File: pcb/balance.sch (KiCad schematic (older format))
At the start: 41 parts, among them J1 Resistive_Touch, J2 JTAG, J3 Conn_01x04_Male, J4 PJ-102AH, J5 UART (Bluetooth), J6 Conn_02x03_Top_Bottom, J7 Conn_02x03_Top_Bottom, M1 Motor_Servo, M2 Motor_Servo, Q1 MMBT3904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

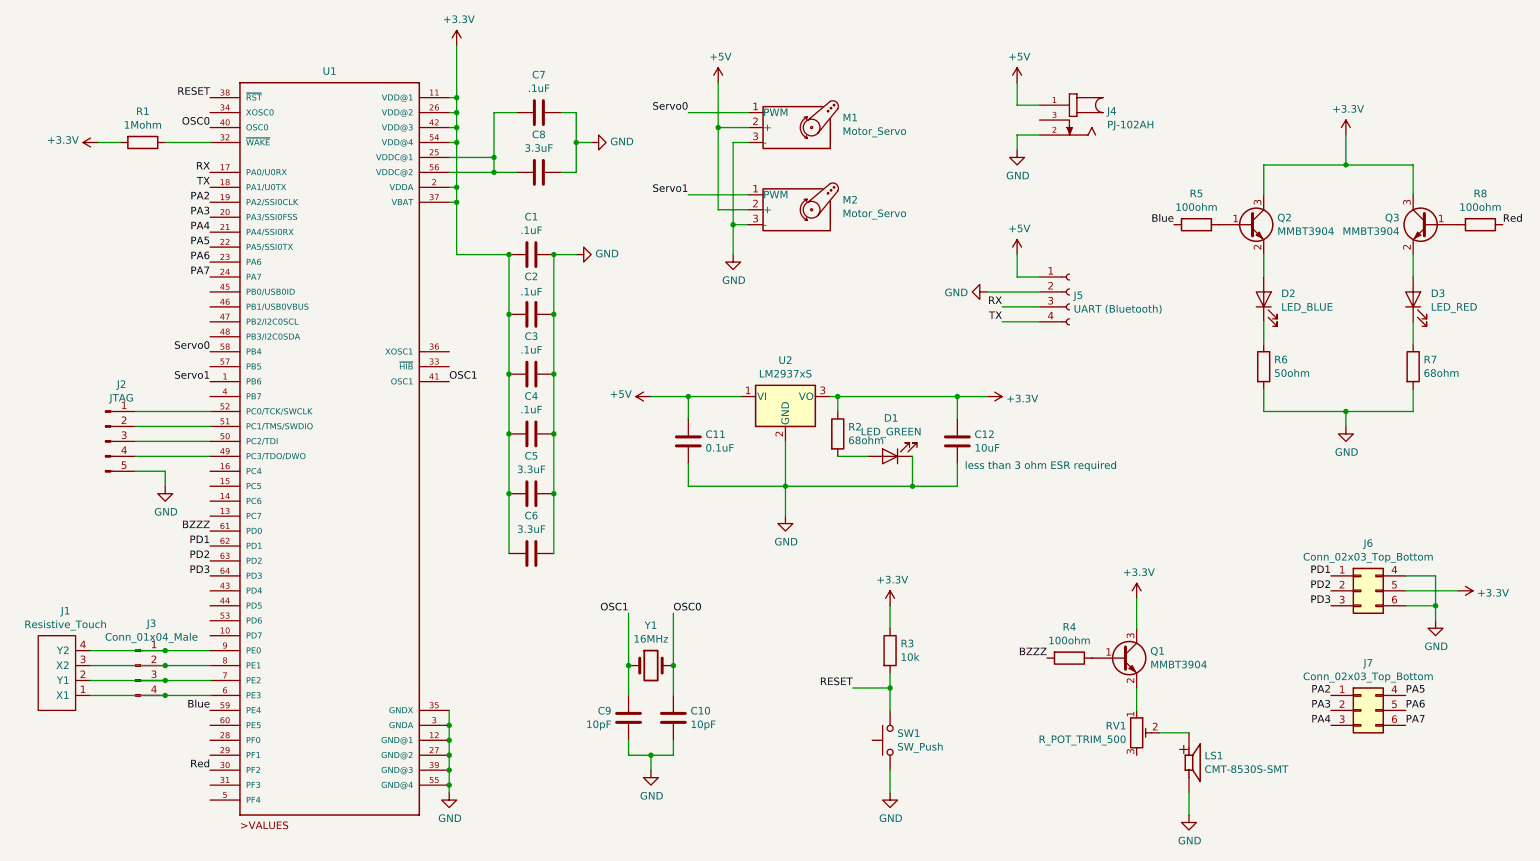
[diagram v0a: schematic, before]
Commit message: Modify component placement and fix transistor circuits
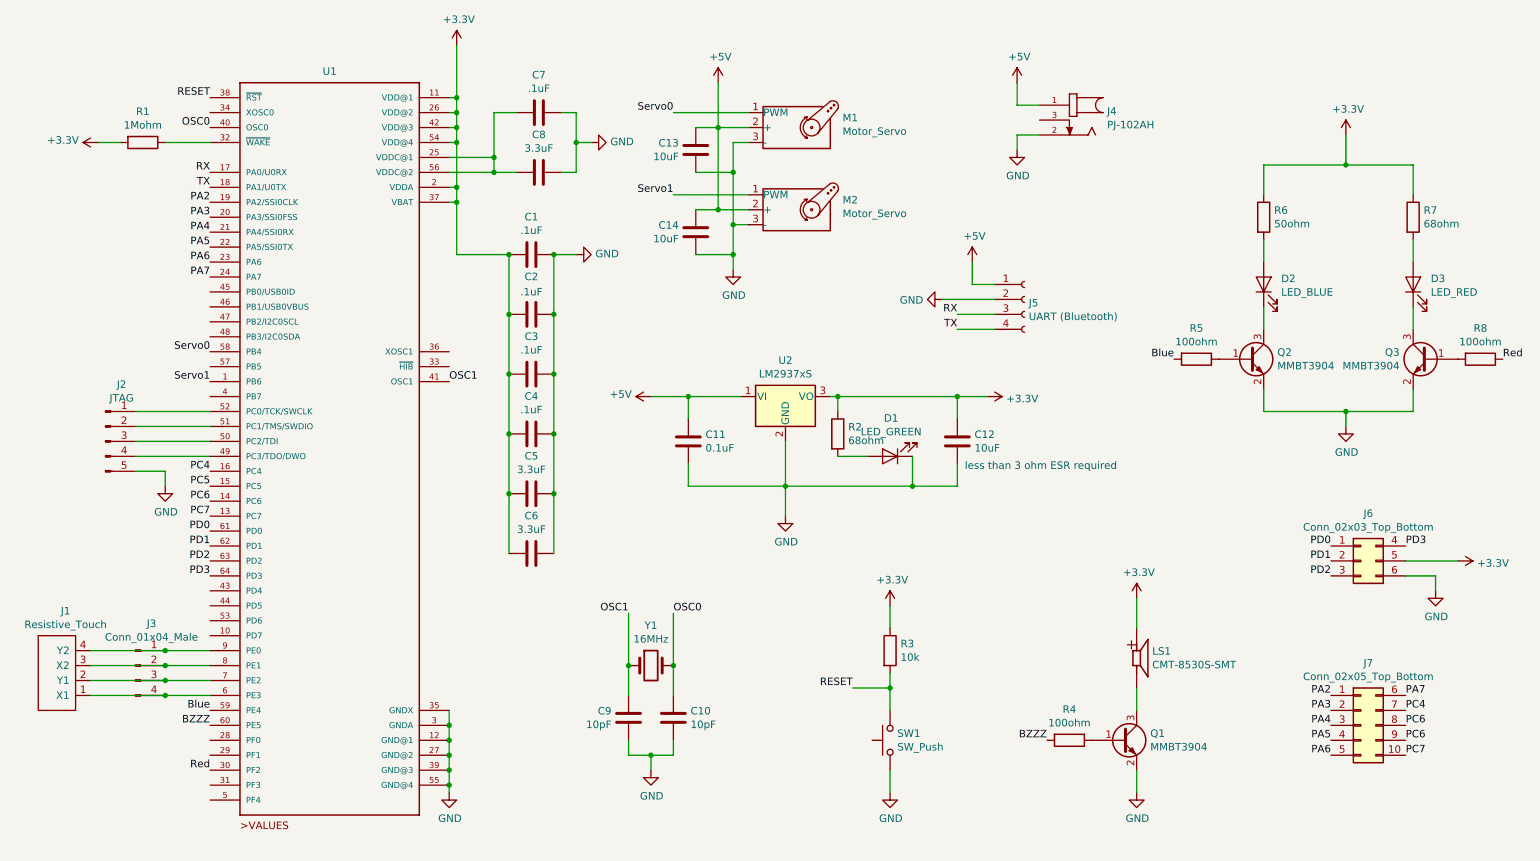
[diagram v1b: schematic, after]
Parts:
- removed J7: Conn_02x03_Top_Bottom, Connector_PinHeader_2.54mm:PinHeader_2x03_P2.54mm_Vertical, symbol Connector_Generic:Conn_02x03_Top_Bottom
- removed RV1: R_POT_TRIM_500, Potentiometer_SMD:Potentiometer_Bourns_3314J_Vertical, symbol Device:R_POT_TRIM
- added C13, C14: 10uF, Capacitor_SMD:C_0805_2012Metric, symbol Device:C
- added J7: Conn_02x05_Top_Bottom, Connector_PinHeader_2.54mm:PinHeader_2x05_P2.54mm_Vertical, symbol Connector_Generic:Conn_02x05_Top_Bottom
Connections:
- net +3V3: now also LS1.P, R6.1, R7.1; no longer Q1.3 (C), Q2.3 (C), Q3.3 (C)
- net +5V: now also C13.2, C14.2
- net BZZZ: now also U1.60 (PE5); no longer U1.61 (PD0)
- net GND: now also Q1.2 (E), Q2.2 (E), Q3.2 (E), C13.1, C14.1; no longer J6.4 (Pin_4), LS1.N, R6.2, R7.2
- net PA2: now also J7.1 (Pin_1)
- net PA3: now also J7.2 (Pin_2)
- net PA4: now also J7.3 (Pin_3)
- net PA5: now also J7.4 (Pin_4)
- net PA6: now also J7.5 (Pin_5)
- net PA7: now also J7.6 (Pin_6)
- net PD1: now also J6.2 (Pin_2); no longer J6.1 (Pin_1)
- net PD2: now also J6.3 (Pin_3); no longer J6.2 (Pin_2)
- net PD3: now also J6.4 (Pin_4); no longer J6.3 (Pin_3)
- net PC7: now reaches U1.13 (PC7)
- net PC7: now also J7.10 (Pin_10)
- net PC6: now reaches U1.14 (PC6)
- net PC6: now also J7.8 (Pin_8), J7.9 (Pin_9)
- net PC5: now reaches U1.15 (PC5)
- net PC4: now reaches U1.16 (PC4)
- net PC4: now also J7.7 (Pin_7)
- net at D2.2 (A): now also R6.2; no longer Q2.2 (E)
- net at D2.1 (K): now also Q2.3 (C); no longer R6.1
- net at D3.2 (A): now also R7.2; no longer Q3.2 (E)
- net at D3.1 (K): now also Q3.3 (C); no longer R7.1
- new net: LS1.N, Q1.3 (C)
- new net PD0: J6.1 (Pin_1), U1.61 (PD0)
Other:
- moved on the sheet: D2, D3, J5, J6, LS1, Q1, Q2, Q3, R4, R5, R6, R7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

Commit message: Route the board
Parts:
- removed J4: PJ-102AH, PJ-102AH:CUI_PJ-102AH, symbol PJ-102AH:PJ-102AH
- added J4: Barrel_Jack_Switch, Connector_BarrelJack:BarrelJack_CUI_PJ-102AH_Horizontal, symbol Connector:Barrel_Jack_Switch
- J5: footprint Connector_PinSocket_2.54mm:PinSocket_1x04_P2.54mm_Horizontal -> Connector_PinSocket_2.54mm:PinSocket_1x04_P2.54mm_Vertical
- LS1: symbol CMT-8530S-SMT:CMT-8530S-SMT -> balance-rescue:CMT-8530S-SMT-CMT-8530S-SMT
- U1: symbol TM4C123GH6PMI:TM4C123GH6PMI -> balance-rescue:TM4C123GH6PMI-TM4C123GH6PMI
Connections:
- net +5V: now also J4.1
- net GND: now also J4.2
- net PC5: now also J7.8 (Pin_8)
- net PC6: no longer J7.8 (Pin_8)
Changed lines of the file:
@@
 $EndDescr
 $Comp
-L TM4C123GH6PMI:TM4C123GH6PMI U1
+L balance-rescue:TM4C123GH6PMI-TM4C123GH6PMI U1
 U 1 1 5DB37352
 P 2800 3550
@@
 Wire Wire Line
 	5850 3850 5850 4050
-Text Notes 7050 3750 0    50   ~ 0
-less than 3 ohm ESR required
 Wire Wire Line
 	5850 3850 6700 3850
@@
 F 0 "J5" H 7478 2576 50  0000 L CNN
 F 1 "UART (Bluetooth)" H 7478 2485 50  0000 L CNN
-F 2 "Connector_PinSocket_2.54mm:PinSocket_1x04_P2.54mm_Horizontal" H 7450 2600 50  0001 C CNN
+F 2 "Connector_PinSocket_2.54mm:PinSocket_1x04_P2.54mm_Vertical" H 7450 2600 50  0001 C CNN
 F 3 "~" H 7450 2600 50  0001 C CNN
 	1    7450 2600
@@
 $EndComp
 $Comp
-L CMT-8530S-SMT:CMT-8530S-SMT LS1
+L balance-rescue:CMT-8530S-SMT-CMT-8530S-SMT LS1
 U 1 1 5E11A03B
 P 8200 5000
@@
 Text Label 2000 1250 2    50   ~ 0
 RESET
-$Comp
-L PJ-102AH:PJ-102AH J4
-U 1 1 5E185784
-P 7750 1400
-F 0 "J4" H 7498 1459 50  0000 R CNN
-F 1 "PJ-102AH" H 7498 1368 50  0000 R CNN
-F 2 "PJ-102AH:CUI_PJ-102AH" H 7750 1400 50  0001 L BNN
-F 3 "None" H 7750 1400 50  0001 L BNN
-F 4 "2.0 x 6.5 mm, 5.0 A, Horizontal, Through Hole, Tapered Pins, Dc Power Jack Connector" H 7750 1400 50  0001 L BNN "Field4"
-F 5 "PJ-102AH" H 7750 1400 50  0001 L BNN "Field5"
-F 6 "Unavailable" H 7750 1400 50  0001 L BNN "Field6"
-F 7 "https://www.cuidevices.com/product/interconnect/connectors/dc-power-connectors/jacks/pj-102ah?utm_source=snapeda.com&utm_medium=referral&utm_campaign=snapedaBOM" H 7750 1400 50  0001 L BNN "Field7"
-F 8 "None" H 7750 1400 50  0001 L BNN "Field8"
-F 9 "CUI Devices" H 7750 1400 50  0001 L BNN "Field9"
-	1    7750 1400
-	-1   0    0    -1
-$EndComp
 $Comp
 L Connector_Generic:Conn_02x03_Top_Bottom J6
@@
 PC4
 Text Label 10000 5450 0    50   ~ 0
-PC6
+PC5
 Text Label 10000 5550 0    50   ~ 0
 PC6
 Text Label 10000 5650 0    50   ~ 0
 PC7
+$Comp
+L Connector:Barrel_Jack_Switch J4
+U 1 1 5DC06347
+P 7850 1400
+F 0 "J4" H 7620 1442 50  0000 R CNN
+F 1 "Barrel_Jack_Switch" H 7620 1351 50  0000 R CNN
+F 2 "Connector_BarrelJack:BarrelJack_CUI_PJ-102AH_Horizontal" H 7900 1360 50  0001 C CNN
+F 3 "~" H 7900 1360 50  0001 C CNN
+	1    7850 1400
+	-1   0    0    -1
+$EndComp
+Text Notes 7050 3750 0    50   ~ 0
+less than 3 ohm ESR required
 $EndSCHEMATC
